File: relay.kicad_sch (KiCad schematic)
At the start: 19 parts, among them J4 Screw, J5 Screw, J6 Screw, J7 Screw, Q2 BC847, Q3 BC847, Q4 TIP127, U4 PC817, U5 PC817, U6 PC817

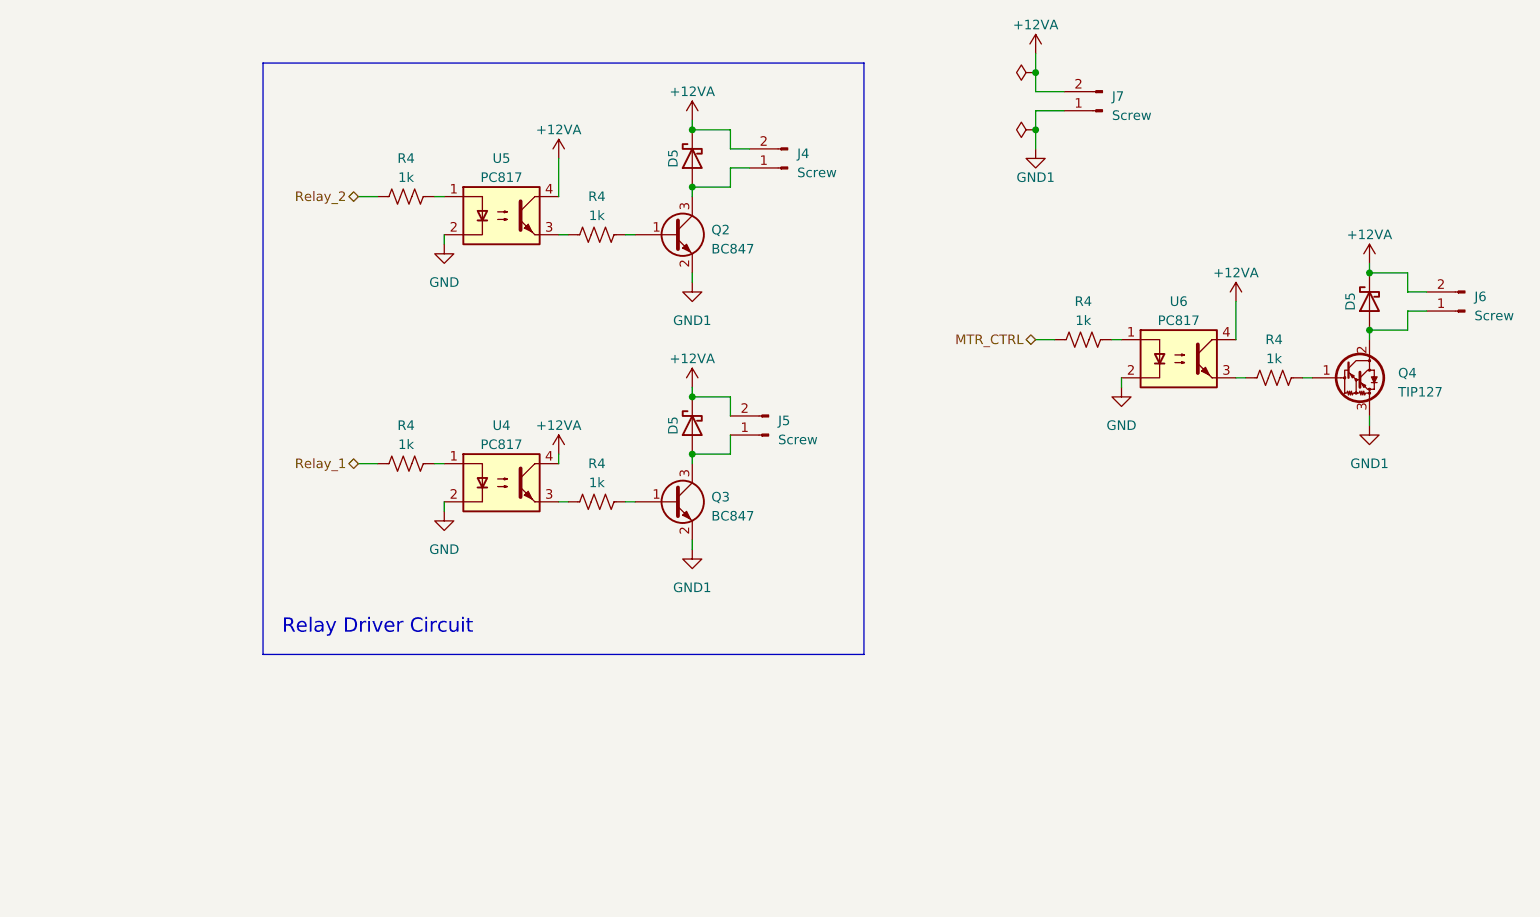
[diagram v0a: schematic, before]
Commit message: Designed circuit for reading digital input. CHY74 (4 channel optocoupler) used
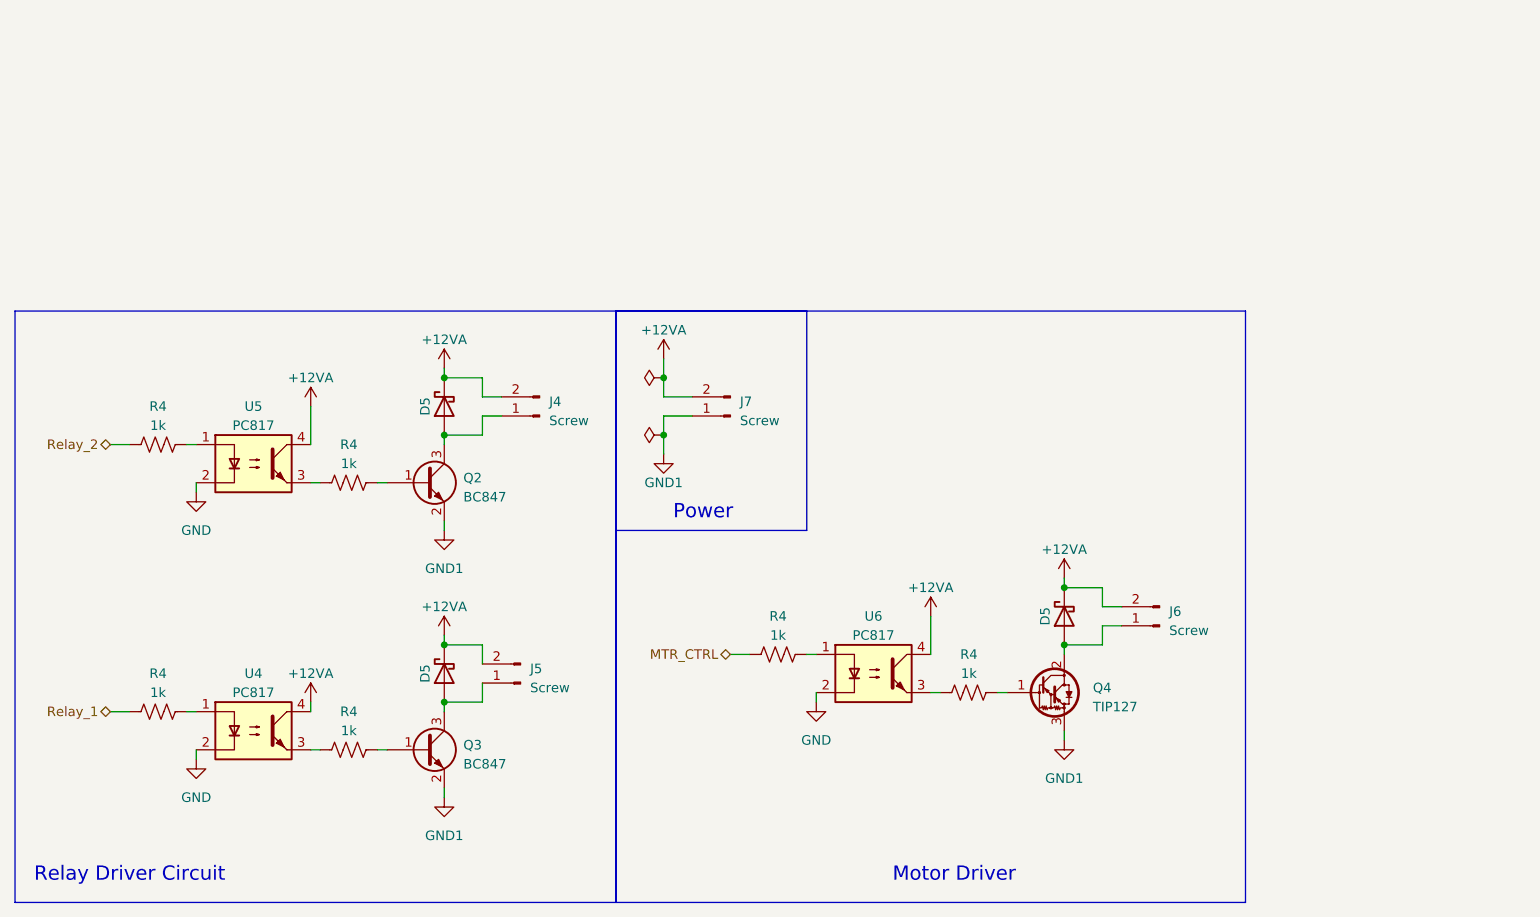
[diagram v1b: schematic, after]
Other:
- note added: "Motor Driver"
- note added: "Power"
- moved on the sheet: D5, J4, J5, J6, J7, Q2, Q3, Q4, R4, U4, U5, U6
